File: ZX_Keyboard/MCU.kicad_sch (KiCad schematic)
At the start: 18 parts, among them J1 DBG_UART, SW1 RESET, U1 STM32F105R8Tx, Y1 Crystal

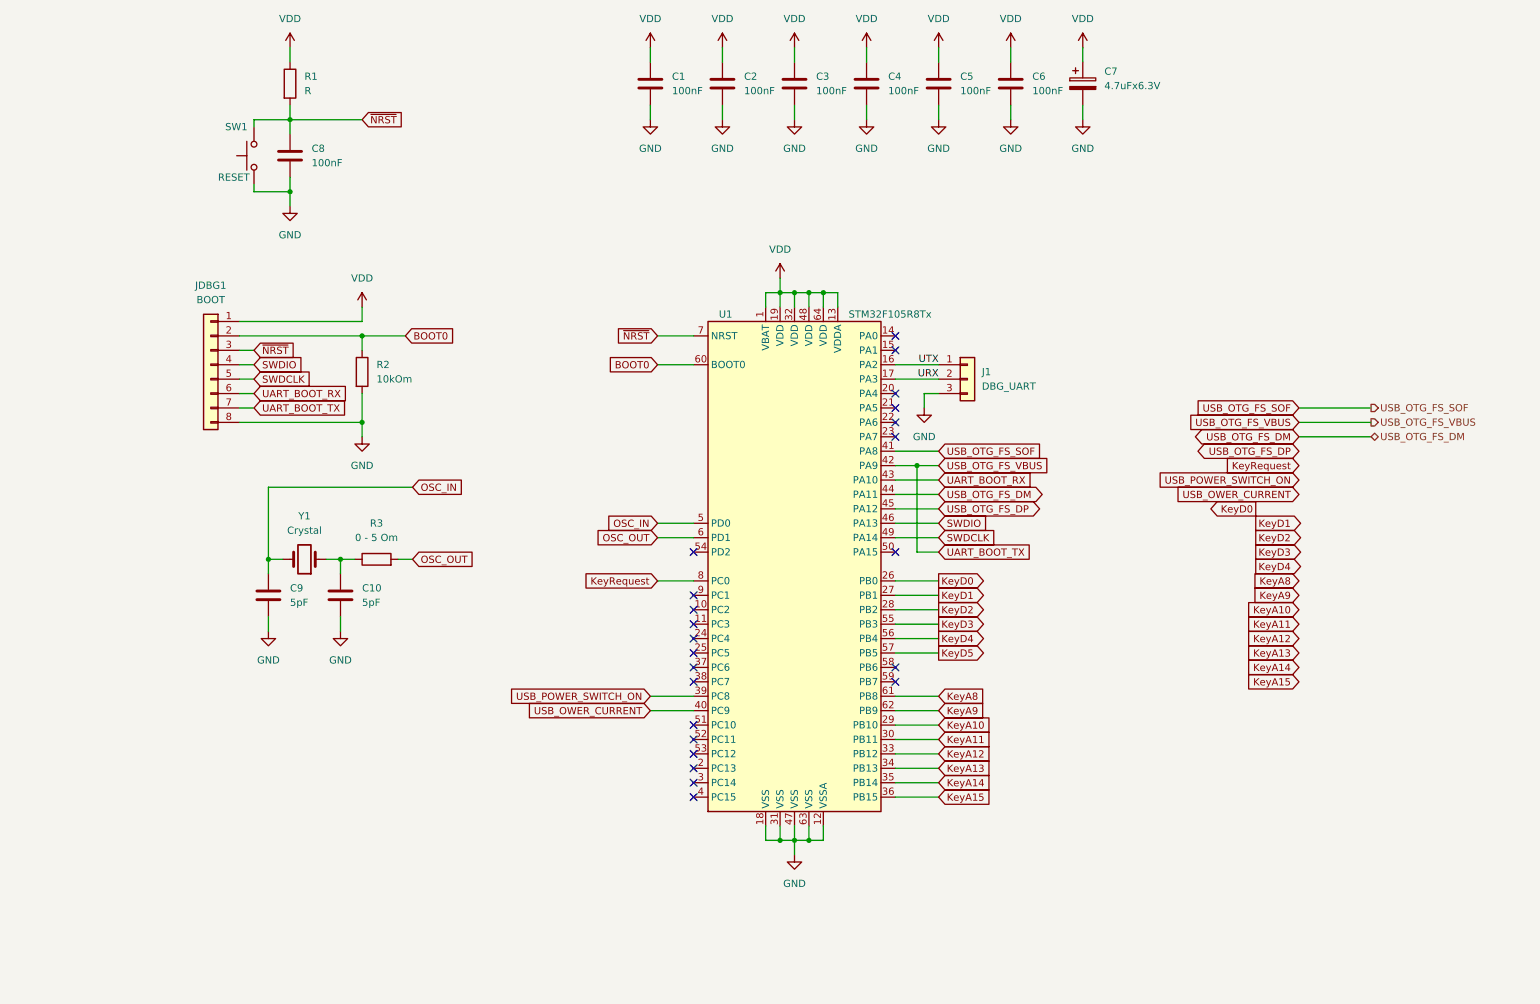
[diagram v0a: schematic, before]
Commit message: add connector sheet
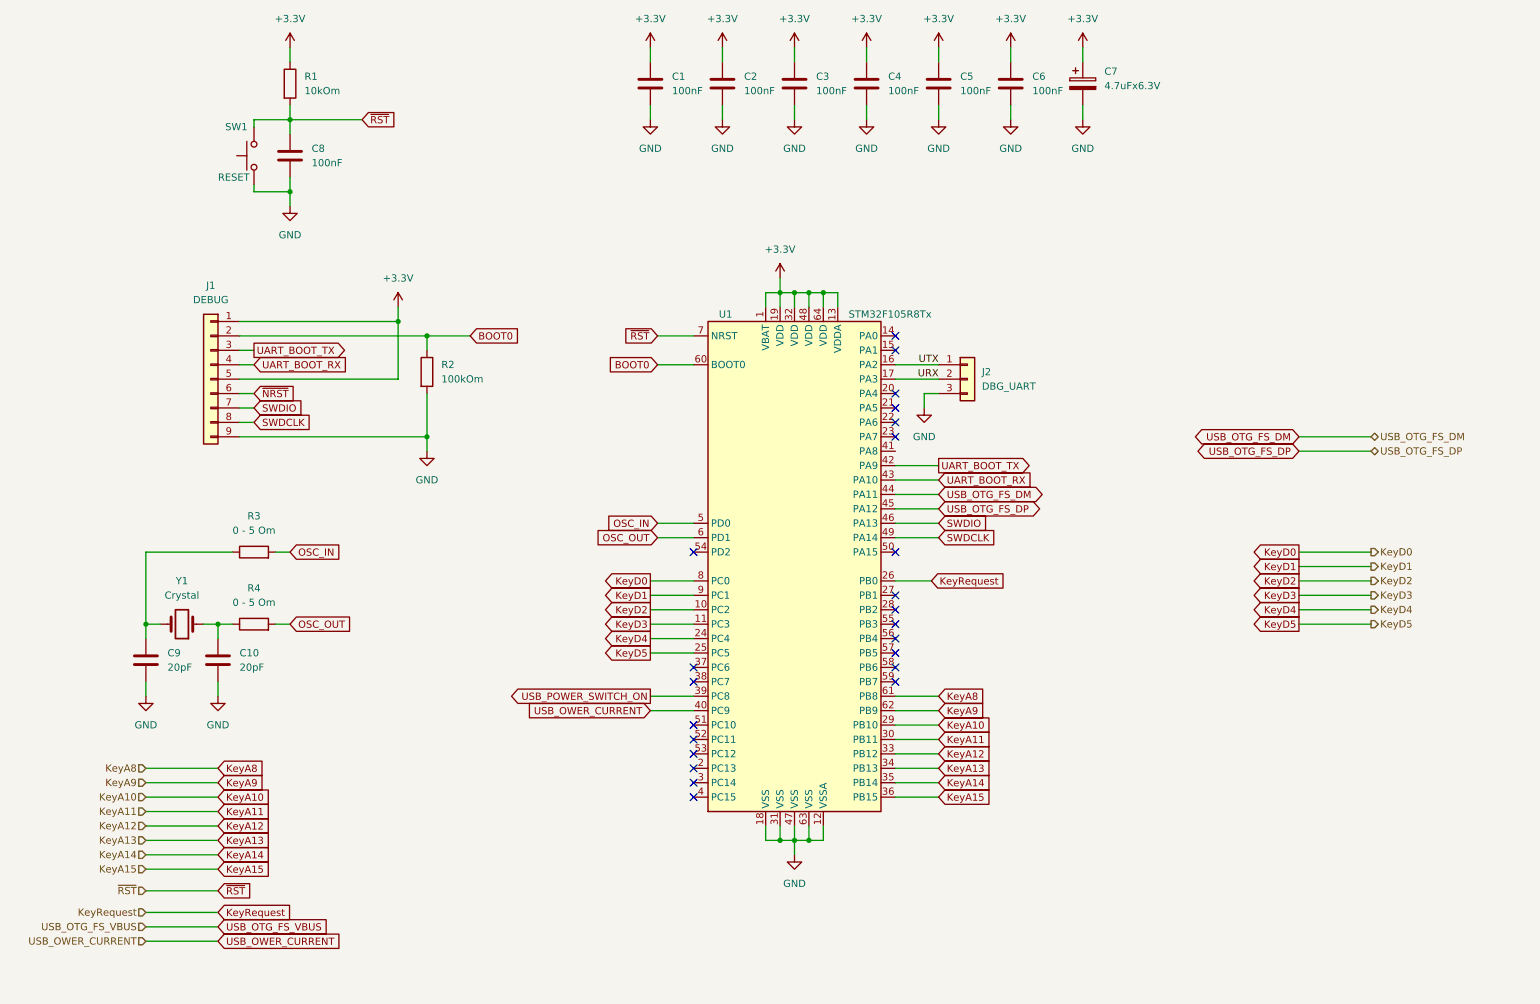
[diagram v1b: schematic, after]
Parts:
- removed JDBG1: BOOT, Connector_PinHeader_2.54mm:PinHeader_1x08_P2.54mm_Vertical, symbol Connector_Generic:Conn_01x08
- added J1: DEBUG, Connector_PinHeader_2.54mm:PinHeader_1x09_P2.54mm_Vertical, symbol Connector_Generic:Conn_01x09
- added R3: 0 - 5 Om, Resistor_SMD:R_0805_2012Metric_Pad1.20x1.40mm_HandSolder, symbol Device:R
- C10, C9: value 5pF -> 20pF
- R1: value R -> 10kOm
- R2: value 10kOm -> 100kOm
- renumbered J1 to J2, R3 to R4
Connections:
- net BOOT0: now also J1.2 (Pin_2)
- net GND: now also J1.9 (Pin_9)
- net KeyD0: now also U1.8 (PC0); no longer U1.26 (PB0)
- net KeyD1: now also U1.9 (PC1); no longer U1.27 (PB1)
- net KeyD2: now also U1.10 (PC2); no longer U1.28 (PB2)
- net KeyD3: now also U1.11 (PC3); no longer U1.55 (PB3)
- net KeyD4: now also U1.24 (PC4); no longer U1.56 (PB4)
- net KeyD5: now also U1.25 (PC5); no longer U1.57 (PB5)
- net KeyRequest: now also U1.26 (PB0); no longer U1.8 (PC0)
- net OSC_IN: now also R3.2; no longer C9.1, Y1.2
- net SWDCLK: now also J1.8 (Pin_8)
- net SWDIO: now also J1.7 (Pin_7)
- net UART_BOOT_RX: now also J1.4 (Pin_4)
- net UART_BOOT_TX: now also J1.3 (Pin_3)
- net ~{NRST}: now also J1.6 (Pin_6); no longer C8.1, R1.2, SW1.2, U1.7 (NRST)
- net USB_OTG_FS_SOF: no longer names the net of U1.41 (PA8)
- net VDD renamed +3.3V
- net +3.3V: now also J1.1 (Pin_1), J1.5 (Pin_5)
- new net: C9.1, R3.1, Y1.2
- new net ~{RST}: C8.1, R1.2, SW1.2, U1.7 (NRST)
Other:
- title: (none) -> USB_Keyboard for ZX-Spectrum
- moved on the sheet: C10, C9, R2, R4, Y1

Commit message: improve zx_keyboard schematic
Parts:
- renumbered J2 to J1, J1 to J2
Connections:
- net KeyA10: no longer names the net of U1.29 (PB10)
- net KeyA11: no longer names the net of U1.30 (PB11)
- net KeyA12: no longer names the net of U1.33 (PB12)
- net KeyA13: no longer names the net of U1.34 (PB13)
- net KeyA14: no longer names the net of U1.35 (PB14)
- net KeyA15: no longer names the net of U1.36 (PB15)
- net KeyA8: no longer names the net of U1.61 (PB8)
- net KeyA9: no longer names the net of U1.62 (PB9)
- net KeyD0: no longer names the net of U1.8 (PC0)
- net KeyD1: no longer names the net of U1.9 (PC1)
- net KeyD2: no longer names the net of U1.10 (PC2)
- net KeyD3: no longer names the net of U1.11 (PC3)
- net KeyD4: no longer names the net of U1.24 (PC4)
- net KeyD5: no longer names the net of U1.25 (PC5)
- net KeyRequest: no longer names the net of U1.26 (PB0)
- no-connect marks 23 -> 38
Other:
- moved on the sheet: J2, R2

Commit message: improve schematic
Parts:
- Y1: value Crystal -> 8MHz
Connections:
- net LOAD: now reaches U1.20 (PA4)
- net SCK: now reaches U1.21 (PA5)
- net CLEAR: now reaches U1.22 (PA6)
- net MOIS: now reaches U1.23 (PA7)
- no-connect marks 38 -> 35
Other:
- moved on the sheet: J1

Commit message: update and fix schematic
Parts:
- added D1, D2: 1N4001, symbol Device:D
- renumbered R3 to R2, R4 to R3, R2 to R4
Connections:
- net ~{NRST} is gone; now on net ~{RST}: J2.6 (Pin_6)
- net +3.3V: no longer J2.5 (Pin_5)
- net ~{RST}: now also D1.1 (K); no longer R1.2, U1.7 (NRST)
- net at U1.54 (PD2): now also D2.1 (K)
- new net: D1.2 (A), D2.2 (A), R1.2, U1.7 (NRST)
- new net VIN+5V: J2.5 (Pin_5)
- no-connect marks 35 -> 34
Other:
- moved on the sheet: C8, J2, R1, R4, SW1

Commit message: add footprint for D1 D2 MCU unit
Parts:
- D1, D2: footprint (none) -> Diode_SMD:D_SOD-523
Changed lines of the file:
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@@
       (effects (font (size 1.27 1.27)) (justify right))
     )
-    (property "Footprint" "" (id 2) (at 116.205 92.075 0)
+    (property "Footprint" "Diode_SMD:D_SOD-523" (id 2) (at 116.205 92.075 0)
       (effects (font (size 1.27 1.27)) hide)
     )
@@
     (property "Reference" "D1" (id 0) (at 105.41 69.85 0))
     (property "Value" "1N4001" (id 1) (at 105.41 72.39 0))
-    (property "Footprint" "" (id 2) (at 105.41 76.2 0)
-      (effects (font (size 1.27 1.27)) hide)
-    )
+    (property "Footprint" "Diode_SMD:D_SOD-523" (id 2) (at 105.41 76.2 0)
+      (effects (font (size 1.27 1.27)) hide)
+    )

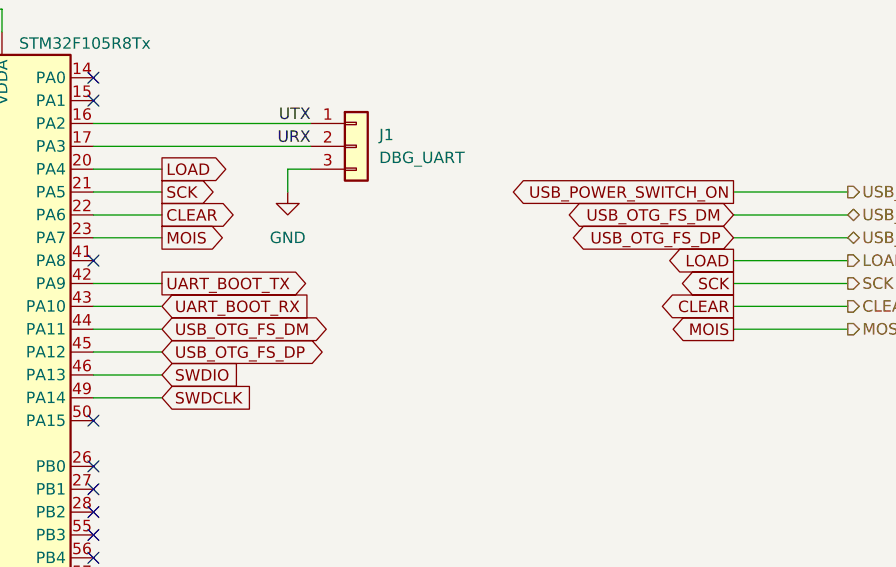
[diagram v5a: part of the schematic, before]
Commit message: rename from MOIS to MOSI
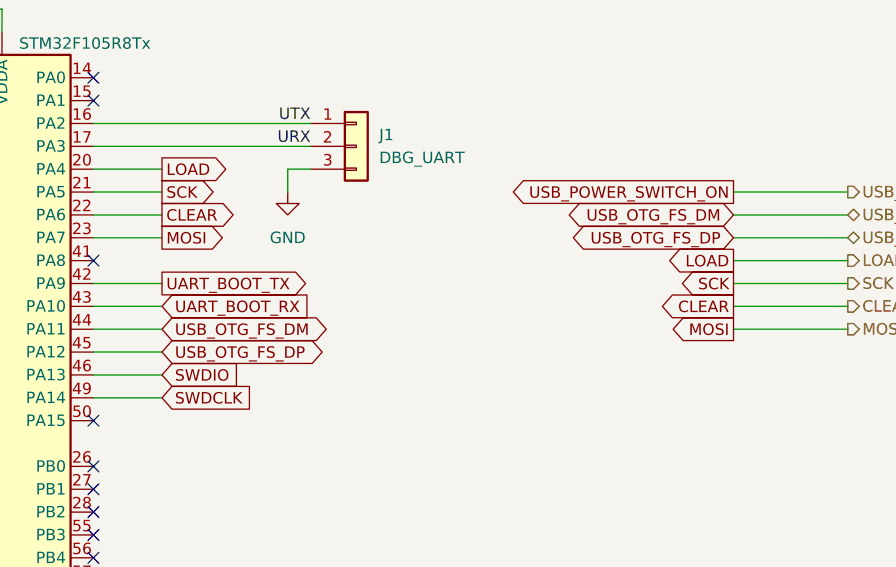
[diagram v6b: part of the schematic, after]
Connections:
- net MOIS renamed MOSI
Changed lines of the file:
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@@
     )
   )
-  (global_label "MOIS" (shape output) (at 177.8 93.98 0) (fields_autoplaced)
+  (global_label "MOSI" (shape output) (at 177.8 93.98 0) (fields_autoplaced)
     (effects (font (size 1.27 1.27)) (justify left))
     (property "Intersheet References" "${INTERSHEET_REFS}" (id 0) (at 184.8093 93.9006 0)
@@
     )
   )
-  (global_label "MOIS" (shape output) (at 241.3 104.14 180) (fields_autoplaced)
+  (global_label "MOSI" (shape output) (at 241.3 104.14 180) (fields_autoplaced)
     (effects (font (size 1.27 1.27)) (justify right))
     (property "Intersheet References" "${INTERSHEET_REFS}" (id 0) (at 234.2907 104.0606 0)

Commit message: update schematic and pcb
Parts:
- C7: footprint Capacitor_Tantalum_SMD:CP_EIA-3528-21_Kemet-B_Pad1.50x2.35mm_HandSolder -> Capacitor_Tantalum_SMD:CP_EIA-3216-18_Kemet-A_Pad1.58x1.35mm_HandSolder
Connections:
- net USB_OWER_CURRENT: now also U1.39 (PC8); no longer U1.40 (PC9)
- net USB_POWER_SWITCH_ON: now also U1.40 (PC9); no longer U1.39 (PC8)
- net USB_OTG_FS_DM renamed USB_OTG_FS_DM-
- net USB_OTG_FS_DP renamed USB_OTG_FS_DP+

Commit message: update pcb
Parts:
- added J3: BOOT2, Connector_PinHeader_2.54mm:PinHeader_1x02_P2.54mm_Vertical, symbol Connector_Generic:Conn_01x02
- added R5: 10kOm, Resistor_SMD:R_0805_2012Metric_Pad1.20x1.40mm_HandSolder, symbol Device:R
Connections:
- net +3.3V: now also J3.1 (Pin_1)
- net GND: now also R5.2
- net BOOT2: now reaches U1.41 (PA8)
- net BOOT2: now also J3.2 (Pin_2), R5.1
- no-connect marks 34 -> 33
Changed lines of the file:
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@@
   (junction (at 154.94 68.58) (diameter 0) (color 0 0 0 0)
+  )
+  (junction (at 113.03 172.72) (diameter 0) (color 0 0 0 0)
   )
   (junction (at 154.94 165.1) (diameter 0) (color 0 0 0 0)
@@
   (no_connect (at 134.62 144.78))
   (no_connect (at 170.18 127))
-  (no_connect (at 170.18 96.52))
   (no_connect (at 170.18 142.24))
   (no_connect (at 134.62 119.38))
@@
     (stroke (width 0) (type default) (color 0 0 0 0))
   )
+  (wire (pts (xy 113.03 172.72) (xy 119.38 172.72))
+    (stroke (width 0) (type default) (color 0 0 0 0))
+  )
   (wire (pts (xy 50.8 127) (xy 50.8 129.54))
     (stroke (width 0) (type default) (color 0 0 0 0))
@@
     (stroke (width 0) (type default) (color 0 0 0 0))
   )
+  (wire (pts (xy 116.84 167.64) (xy 116.84 170.18))
+    (stroke (width 0) (type default) (color 0 0 0 0))
+  )
   (wire (pts (xy 50.8 137.16) (xy 50.8 139.7))
     (stroke (width 0) (type default) (color 0 0 0 0))
@@
     (stroke (width 0) (type default) (color 0 0 0 0))
   )
+  (wire (pts (xy 116.84 170.18) (xy 119.38 170.18))
+    (stroke (width 0) (type default) (color 0 0 0 0))
+  )
   (wire (pts (xy 241.3 93.98) (xy 254 93.98))
     (stroke (width 0) (type default) (color 0 0 0 0))
   )
+  (wire (pts (xy 113.03 172.72) (xy 113.03 175.26))
+    (stroke (width 0) (type default) (color 0 0 0 0))
+  )
   (wire (pts (xy 152.4 165.1) (xy 154.94 165.1))
     (stroke (width 0) (type default) (color 0 0 0 0))
@@
     (stroke (width 0) (type default) (color 0 0 0 0))
   )
+  (wire (pts (xy 106.68 172.72) (xy 113.03 172.72))
+    (stroke (width 0) (type default) (color 0 0 0 0))
+  )
   (wire (pts (xy 147.32 165.1) (xy 149.86 165.1))
     (stroke (width 0) (type default) (color 0 0 0 0))
@@
     (stroke (width 0) (type default) (color 0 0 0 0))
   )
+  (wire (pts (xy 113.03 182.88) (xy 113.03 185.42))
+    (stroke (width 0) (type default) (color 0 0 0 0))
+  )
   (wire (pts (xy 190.5 35.56) (xy 190.5 38.1))
     (stroke (width 0) (type default) (color 0 0 0 0))
@@
   )
   (wire (pts (xy 170.18 93.98) (xy 177.8 93.98))
+    (stroke (width 0) (type default) (color 0 0 0 0))
+  )
+  (wire (pts (xy 170.18 96.52) (xy 177.8 96.52))
     (stroke (width 0) (type default) (color 0 0 0 0))
   )
@@
     )
   )
+  (global_label "BOOT2" (shape input) (at 177.8 96.52 0) (fields_autoplaced)
+    (effects (font (size 1.27 1.27)) (justify left))
+    (property "Intersheet References" "${INTERSHEET_REFS}" (id 0) (at 186.3212 96.4406 0)
+      (effects (font (size 1.27 1.27)) (justify left) hide)
+    )
+  )
   (global_label "OSC_IN" (shape input) (at 63.5 114.3 0) (fields_autoplaced)
     (effects (font (size 1.27 1.27)) (justify left))
@@
     (effects (font (size 1.27 1.27)) (justify right))
     (property "Intersheet References" "${INTERSHEET_REFS}" (id 0) (at 216.2083 88.8206 0)
+      (effects (font (size 1.27 1.27)) (justify right) hide)
+    )
+  )
+  (global_label "BOOT2" (shape input) (at 106.68 172.72 180) (fields_autoplaced)
+    (effects (font (size 1.27 1.27)) (justify right))
+    (property "Intersheet References" "${INTERSHEET_REFS}" (id 0) (at 98.1588 172.6406 0)
       (effects (font (size 1.27 1.27)) (justify right) hide)
     )
@@
     (pin "2")
   )
+  (symbol (lib_id "Connector_Generic:Conn_01x02") (at 124.46 170.18 0) (unit 1)
+    (in_bom yes) (on_board yes) (fields_autoplaced)
+    (property "Reference" "J3" (id 0) (at 127 170.1799 0)
+      (effects (font (size 1.27 1.27)) (justify left))
+    )
+    (property "Value" "BOOT2" (id 1) (at 127 172.7199 0)
+      (effects (font (size 1.27 1.27)) (justify left))
+    )
+    (property "Footprint" "Connector_PinHeader_2.54mm:PinHeader_1x02_P2.54mm_Vertical" (id 2) (at 124.46 170.18 0)
+      (effects (font (size 1.27 1.27)) hide)
+    )
+    (property "Datasheet" "~" (id 3) (at 124.46 170.18 0)
+      (effects (font (size 1.27 1.27)) hide)
+    )
+    (pin "1")
+    (pin "2")
+  )
   (symbol (lib_id "Device:R") (at 57.15 114.3 90) (unit 1)
     (in_bom yes) (on_board yes)
@@
     (pin "1")
   )
+  (symbol (lib_id "power:GND") (at 113.03 185.42 0) (unit 1)
+    (in_bom yes) (on_board yes) (fields_autoplaced)
+    (property "Reference" "#PWR0101" (id 0) (at 113.03 191.77 0)
+      (effects (font (size 1.27 1.27)) hide)
+    )
+    (property "Value" "GND" (id 1) (at 113.03 190.5 0))
+    (property "Footprint" "" (id 2) (at 113.03 185.42 0)
+      (effects (font (size 1.27 1.27)) hide)
+    )
+    (property "Datasheet" "" (id 3) (at 113.03 185.42 0)
+      (effects (font (size 1.27 1.27)) hide)
+    )
+    (pin "1")
+  )
   (symbol (lib_id "power:+3.3V") (at 139.7 25.4 0) (unit 1)
     (in_bom yes) (on_board yes) (fields_autoplaced)
@@
     (pin "2")
   )
+  (symbol (lib_id "Device:R") (at 113.03 179.07 0) (unit 1)
+    (in_bom yes) (on_board yes) (fields_autoplaced)
+    (property "Reference" "R5" (id 0) (at 115.57 177.7999 0)
+      (effects (font (size 1.27 1.27)) (justify left))
+    )
+    (property "Value" "10kOm" (id 1) (at 115.57 180.3399 0)
+      (effects (font (size 1.27 1.27)) (justify left))
+    )
+    (property "Footprint" "Resistor_SMD:R_0805_2012Metric_Pad1.20x1.40mm_HandSolder" (id 2) (at 111.252 179.07 90)
+      (effects (font (size 1.27 1.27)) hide)
+    )
+    (property "Datasheet" "~" (id 3) (at 113.03 179.07 0)
+      (effects (font (size 1.27 1.27)) hide)
+    )
+    (pin "1")
+    (pin "2")
+  )
+  (symbol (lib_id "power:+3.3V") (at 116.84 167.64 0) (unit 1)
+    (in_bom yes) (on_board yes) (fields_autoplaced)
+    (property "Reference" "#PWR027" (id 0) (at 116.84 171.45 0)
+      (effects (font (size 1.27 1.27)) hide)
+    )
+    (property "Value" "+3.3V" (id 1) (at 116.84 162.56 0))
+    (property "Footprint" "" (id 2) (at 116.84 167.64 0)
+      (effects (font (size 1.27 1.27)) hide)
+    )
+    (property "Datasheet" "" (id 3) (at 116.84 167.64 0)
+      (effects (font (size 1.27 1.27)) hide)
+    )
+    (pin "1")
+  )
   (symbol (lib_id "power:GND") (at 127 38.1 0) (unit 1)
